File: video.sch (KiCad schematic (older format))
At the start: 42 parts, among them P1 VIDEO OUT, P11 I²C PORT, P2 RGBHV TEST POINTS, U1 VGA SYNC/JOY BUFFER, U2 VGA RGB BUFFER, U3 E-DDC I²C BUFFER

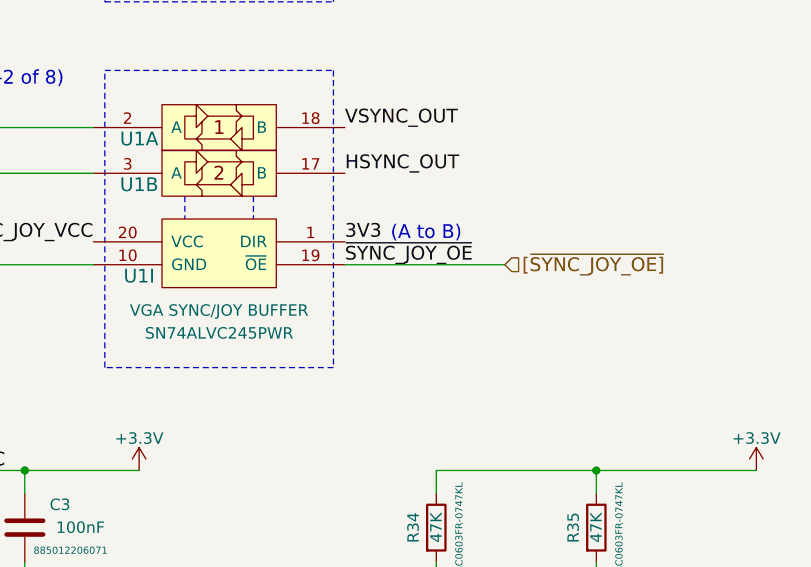
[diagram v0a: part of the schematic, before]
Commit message: Aclaracion menor sobre uso de U1 en diferentes sheets
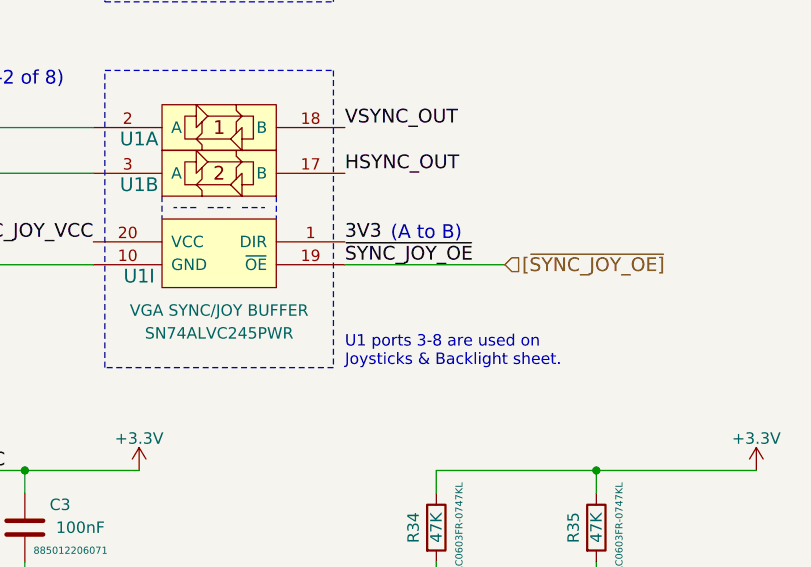
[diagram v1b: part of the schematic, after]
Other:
- note added: "U1 ports 3-8 are used on \nJoysticks & Backlight sheet."
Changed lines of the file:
@@
 	2000 4800 3500 4800
 Wire Notes Line
-	3900 4500 3900 4600
+	3800 4500 3800 4600
 Wire Notes Line
-	4200 4500 4200 4600
+	4300 4500 4300 4600
+Wire Notes Line
+	4000 4550 4100 4550
+Wire Notes Line
+	3950 4550 3850 4550
+Wire Notes Line
+	4150 4550 4250 4550
+Text Notes 4600 5250 0    50   ~ 0
+U1 ports 3-8 are used on \nJoysticks & Backlight sheet.
 $EndSCHEMATC

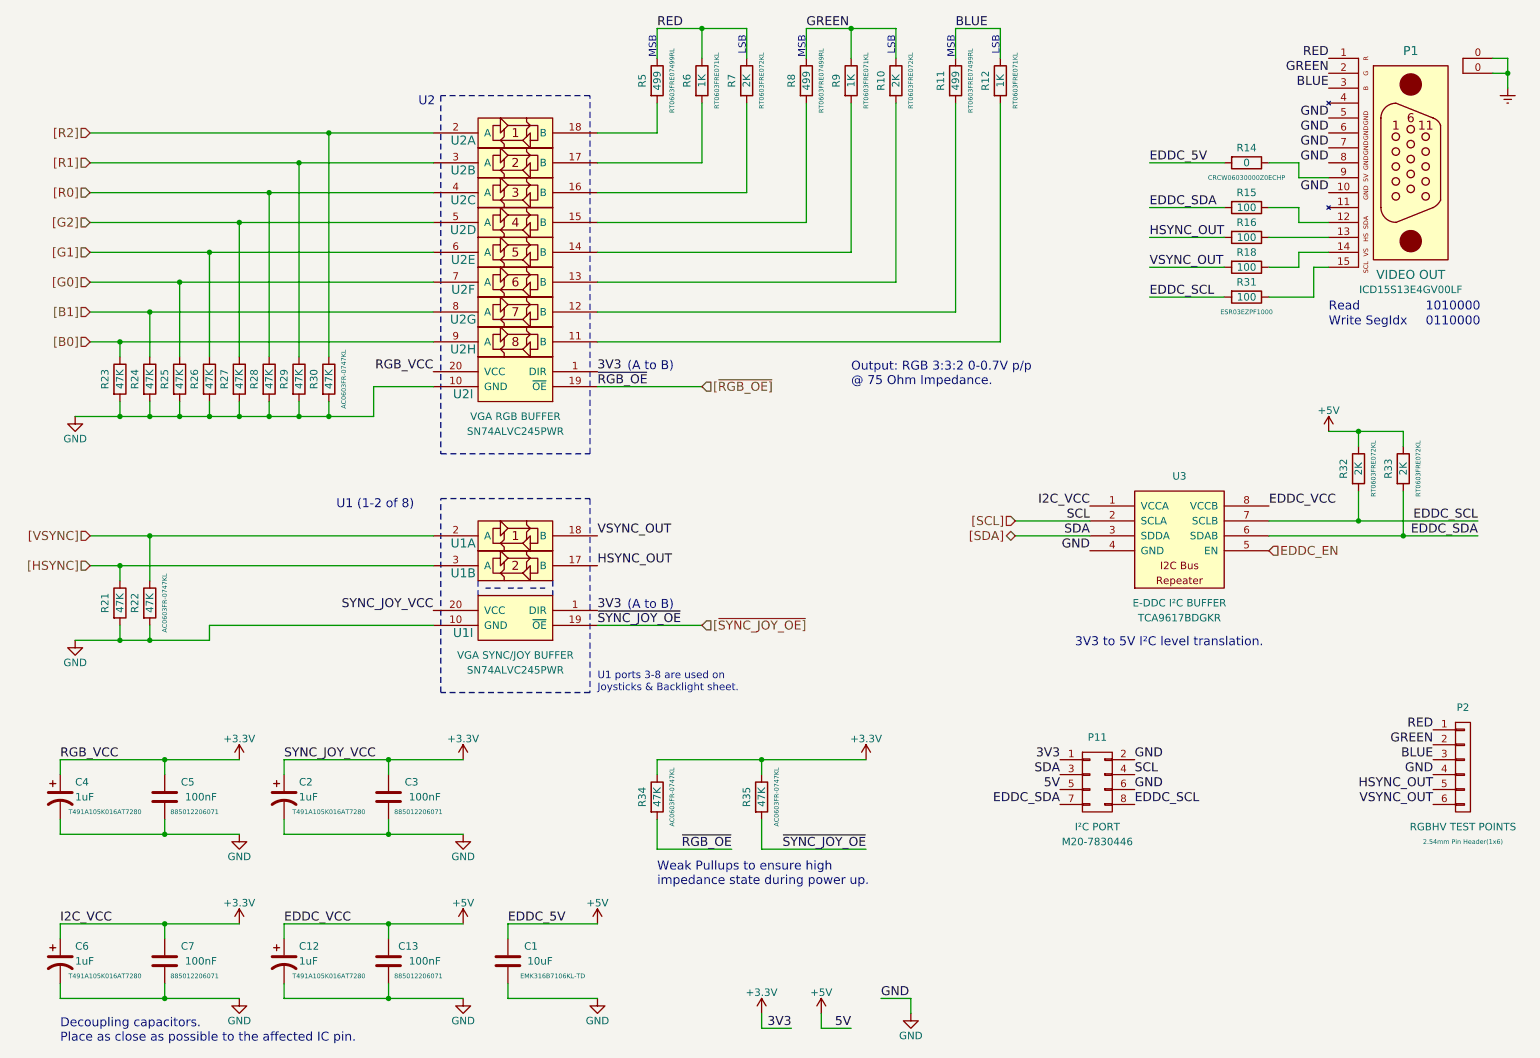
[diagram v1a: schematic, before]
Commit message: Se agrego indice en pagina 1. Union de islas de componentes con cables
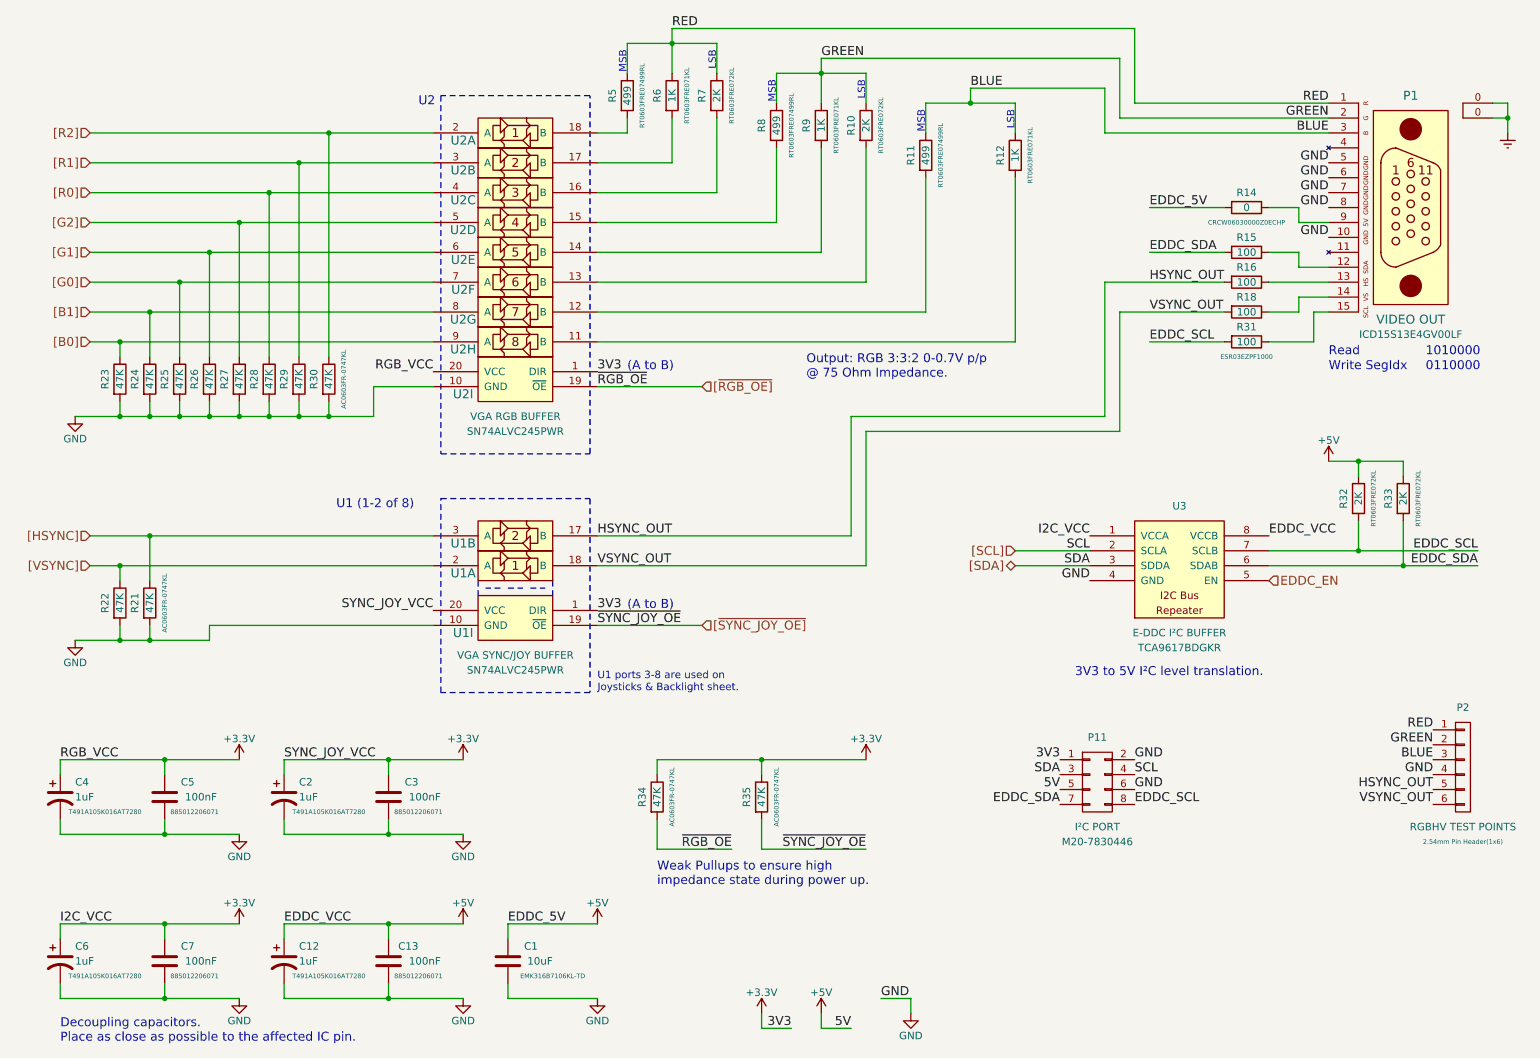
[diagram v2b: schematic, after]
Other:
- moved on the sheet: P1, R10, R11, R12, R14, R15, R16, R18, R21, R22, R31, R32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
